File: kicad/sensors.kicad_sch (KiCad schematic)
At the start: 20 parts, among them J34 Sensors, J35 I2C 5V, U12 PCA9306D

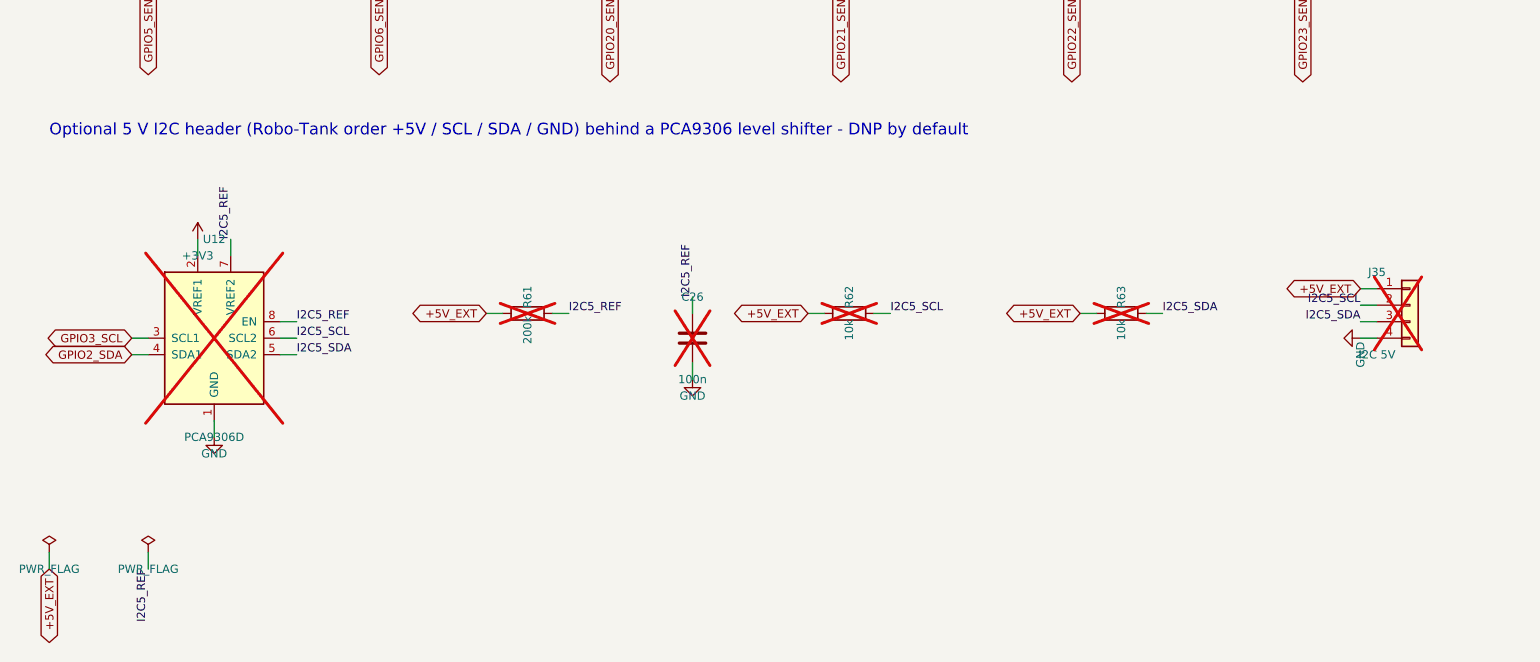
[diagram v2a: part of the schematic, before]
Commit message: kicad: power bar group re-placed and routed, 5 V I2C removed
- Power bars: U10 rotated, RN5..RN8 re-placed, J32/J33 rotated by 180 deg
  (pinout unchanged). Original PCA #2 channel order kept (bar 1 outlet n =
  ch n-1, bar 2 = ch n+7); identical array elements re-assigned in the
  schematic for routing. All power bar nets routed, U10 supply re-done,
  SDA/SCL escape stubs towards the Pi header.
- Sensors: 5 V I2C (PCA9306, J35) removed, I2C is 3.3 V only.
- Board: manual group placement and routing, Q4_DRV clearance fix,
  duplicate via and dangling GND stubs removed.
- README: 5 V I2C note and PCA #2 channel order / rotated headers.

Co-Authored-By: Claude Opus 5.5 <noreply@anthropic.com>
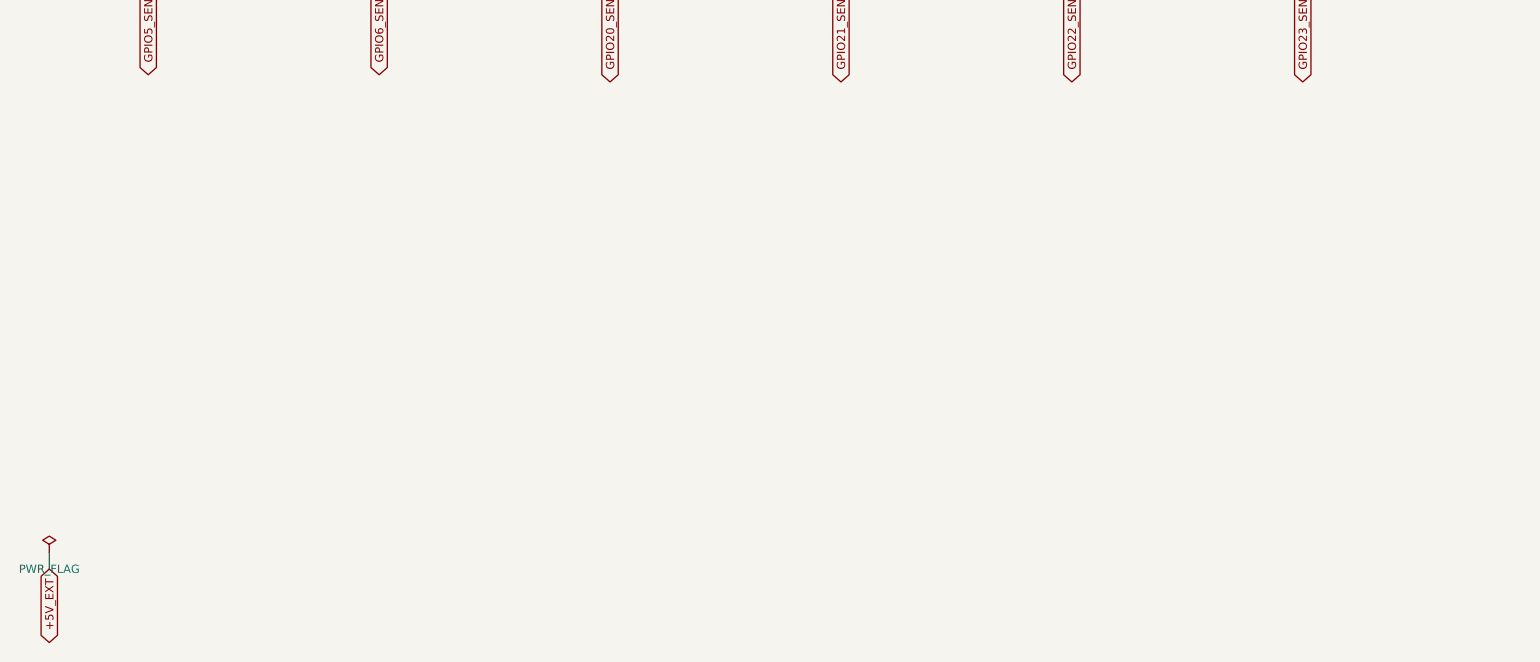
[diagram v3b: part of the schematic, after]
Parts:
- removed C26: 100n, Capacitor_SMD:C_0603_1608Metric, symbol Device:C
- removed J35: I2C 5V, Connector_PinHeader_2.54mm:PinHeader_1x04_P2.54mm_Vertical, symbol Connector_Generic:Conn_01x04
- removed R61: 200k, Resistor_SMD:R_0603_1608Metric, symbol Device:R
- removed R62, R63: 10k, Resistor_SMD:R_0603_1608Metric, symbol Device:R
- removed U12: PCA9306D, Package_SO:SOIC-8_3.9x4.9mm_P1.27mm, symbol Interface:PCA9306D
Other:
- note removed: "Optional 5 V I2C header (Robo-Tank order +5V / SCL / SDA / GND) behind a PCA9306 level shifter - DNP by default"

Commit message: kicad: v2 layout finished - ADC renumbering, port labels, last routes
- ADC sockets numbered 0..3 from right to left; AIN0<->AIN1 and AIN2<->AIN3
  swapped at the ADS1115, U5 end runs re-routed.
- Connector labels: IoRegistry-style port names (PCA#1 chNN, ADC #1 in n,
  GPIO n, DS1820); J5/J6/J8/J9 corrected from GPIO to PCA#1 ch15/14/13/12
  (also in outputs.kicad_sch). Back side: names with voltage/current
  ratings, running from the board edge at pin 1, "+" on supply pins,
  SCL/SDA and 1-Wire Data marks. Front: ADC #1 / in n, jumper labels.
- Routed the last six open nets (+3V3 at J24/JP4, +5V_EXT at J19,
  GPIO2_SDA J22-J23 on B.Cu, AIN1, J24 pin 10 - JP3, PCA1_CH1); PCA1_CH3
  partly moved to B.Cu to free the corridor at U7. Dangling stubs removed.
- Silkscreen: nothing on pads, overlaps reduced with small moves; part
  references and F.Fab texts at 0.8 mm.
- aquaPCB.kicad_dru: the deliberate courtyard overlap of the ADC socket
  pairs J26/J27 and J36/J37 (2.54 mm grid) is waived by a custom rule.

ERC clean, DRC without errors (silkscreen warnings only), board fully
routed and in sync with the schematic.

Co-Authored-By: Claude Opus 5.5 <noreply@anthropic.com>
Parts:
- R55, R56, R57, R58, R59, R60: footprint Resistor_SMD:R_0603_1608Metric -> Resistor_SMD:R_0805_2012Metric; LCSC C21190 -> C17513
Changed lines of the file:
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@@
 			)
 		)
-		(property "Footprint" "Resistor_SMD:R_0603_1608Metric"
+		(property "Footprint" "Resistor_SMD:R_0805_2012Metric"
 			(at 120.65 154.94 0)
 			(hide yes)
@@
 			)
 		)
-		(property "LCSC" "C21190"
+		(property "LCSC" "C17513"
 			(at 120.65 154.94 0)
 			(hide yes)
@@
 			)
 		)
-		(property "Footprint" "Resistor_SMD:R_0603_1608Metric"
+		(property "Footprint" "Resistor_SMD:R_0805_2012Metric"
 			(at 161.29 154.94 0)
 			(hide yes)
@@
 			)
 		)
-		(property "LCSC" "C21190"
+		(property "LCSC" "C17513"
 			(at 161.29 154.94 0)
 			(hide yes)
@@
 			)
 		)
-		(property "Footprint" "Resistor_SMD:R_0603_1608Metric"
+		(property "Footprint" "Resistor_SMD:R_0805_2012Metric"
 			(at 39.37 154.94 0)
 			(hide yes)
@@
 			)
 		)
-		(property "LCSC" "C21190"
+		(property "LCSC" "C17513"
 			(at 39.37 154.94 0)
 			(hide yes)
@@
 			)
 		)
-		(property "Footprint" "Resistor_SMD:R_0603_1608Metric"
+		(property "Footprint" "Resistor_SMD:R_0805_2012Metric"
 			(at 242.57 154.94 0)
 			(hide yes)
@@
 			)
 		)
-		(property "LCSC" "C21190"
+		(property "LCSC" "C17513"
 			(at 242.57 154.94 0)
 			(hide yes)
@@
 			)
 		)
-		(property "Footprint" "Resistor_SMD:R_0603_1608Metric"
+		(property "Footprint" "Resistor_SMD:R_0805_2012Metric"
 			(at 201.93 154.94 0)
 			(hide yes)
@@
 			)
 		)
-		(property "LCSC" "C21190"
+		(property "LCSC" "C17513"
 			(at 201.93 154.94 0)
 			(hide yes)
@@
 			)
 		)
-		(property "Footprint" "Resistor_SMD:R_0603_1608Metric"
+		(property "Footprint" "Resistor_SMD:R_0805_2012Metric"
 			(at 80.01 154.94 0)
 			(hide yes)
@@
 			)
 		)
-		(property "LCSC" "C21190"
+		(property "LCSC" "C17513"
 			(at 80.01 154.94 0)
 			(hide yes)

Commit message: kicad: LCSC numbers for PCA9685 and PTC, status LED names follow PCA#1
- U7/U10 PCA9685PW,118 -> LCSC C2678753, F2 nSMD050 -> C69688 (schematic
  and board), so every assembled part carries an LCSC number.
- Status LEDs D9/D11/D15/D17 renamed GPIO12/13/16/26 -> PCA#1 ch15/14/13/12,
  matching the Q2/Q3/Q5/Q6 drive since v2.

Co-Authored-By: Claude Opus 5.5 <noreply@anthropic.com>
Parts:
- F2: LCSC (none) -> C69688
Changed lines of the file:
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@@
+			)
+		)
+		(property "LCSC" "C69688"
+			(at 25.4 48.26 0)
+			(hide yes)
+			(show_name no)
+			(do_not_autoplace no)
+			(effects
+				(font
+					(size 1.27 1.27)
+				)
 			)
 		)

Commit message: kicad: current paths and thermal fixes in the power section
- 10 VIN vias at the Q10 source (was 6); SW node and 5V_PI widened to 1.5 mm;
  F1 -> Q10 drain widened to 5.5 mm.
- J1 GND pads: local thermal spoke width 1.0 mm (7 spokes into the B.Cu GND plane).
- Q10 drain copper zone (Q10_DRAIN, F.Cu, ~1.25 cm2) for Q10 and the fuse holder.
- Q10 AOD4185 -> DMP4010SK3Q-13 (9.9 mOhm, same DPAK pinout); F1 8 A -> 10 A insert
  (0154010.DR, same holder); F2 PTC 0.5 A -> nSMD110 (1.1 A hold) since the feeder
  shares +5V_EXT.
- B.Cu solder mask opening over the VIN trunk to J4 (optional hand tinning).
- Silkscreen: "max 5A, total 6.5A" on both sides; "12V IN" label nudged off the opening.

ERC clean, DRC without errors, board in sync with the schematic.

Co-Authored-By: Claude Opus 5.5 <noreply@anthropic.com>
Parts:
- F2: value PTC 0.5A -> PTC 1.1A; LCSC C69688 -> C71465
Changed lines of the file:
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@@
 			)
 		)
-		(property "Value" "PTC 0.5A"
+		(property "Value" "PTC 1.1A"
 			(at 25.4 54.61 0)
 			(show_name no)
@@
 			)
 		)
-		(property "LCSC" "C69688"
+		(property "LCSC" "C71465"
 			(at 25.4 48.26 0)
 			(hide yes)
